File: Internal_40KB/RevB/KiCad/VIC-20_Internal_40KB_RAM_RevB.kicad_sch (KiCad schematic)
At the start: 17 parts, among them J1 BLK Decoder, J2 RAM Decoder, J3 Disable/Enable Switch, J4 UD4, J5 UE4, U1 74HCT138, U2 74HCT138, U3 74HCT10, U4 74HCT30, U5 74HCT157, U6 62256

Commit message: Initial Rev B design
A simple extension of the 32KB expansion by adding a 6264 piggybacked on top of the 62256 and routing the ~BLK5 select to it.
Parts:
- added J6: 20, Connector_PinHeader_2.54mm:PinHeader_1x01_P2.54mm_Vertical, symbol Connector_Generic:Conn_01x01
- added J7: 26, Connector_PinHeader_2.54mm:PinHeader_1x01_P2.54mm_Vertical, symbol Connector_Generic:Conn_01x01
- added U7: 6264 SRAM, Package_DIP:DIP-28_W15.24mm, symbol Memory_RAM:HY6264AxP
- C3: value 100nF -> 200nF
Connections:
- net +5V: now also J7.1 (Pin_1), U7.26 (CS2), U7.28 (VCC); no longer U5.14 (I0d)
- net BD0: now also U7.11 (I/O0)
- net BD1: now also U7.12 (I/O1)
- net BD2: now also U7.13 (I/O2)
- net BD3: now also U7.15 (I/O3)
- net BD4: now also U7.16 (I/O4)
- net BD5: now also U7.17 (I/O5)
- net BD6: now also U7.18 (I/O6)
- net BD7: now also U7.19 (I/O7)
- net GND: now also U7.14 (GND)
- net VA0: now also U7.10 (A0)
- net VA1: now also U7.9 (A1)
- net VA10: now also U7.21 (A10)
- net VA11: now also U7.23 (A11)
- net VA12: now also U7.2 (A12)
- net VA2: now also U7.8 (A2)
- net VA3: now also U7.7 (A3)
- net VA4: now also U7.6 (A4)
- net VA5: now also U7.5 (A5)
- net VA6: now also U7.4 (A6)
- net VA7: now also U7.3 (A7)
- net VA8: now also U7.25 (A8)
- net VA9: now also U7.24 (A9)
- net VR/~{W}: now also U7.27 (~{WE})
- net ~{BLK5}: now also U5.14 (I0d), J6.1 (Pin_1), U7.20 (~{CS1}); no longer J1.10 (Pin_10)
- net ~{OE}: now also U7.22 (~{OE})
- net ~{BLK5_{OUT}}: now reaches U5.12 (Zd)
- net ~{BLK5_{OUT}}: now also J1.10 (Pin_10)
- no-connect marks 25 -> 24
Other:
- note removed: "Add ~{BLK5} with additional 6264 in future?"
- title: Commodore VIC-20 32KB RAM Expansion  -> Commodore VIC-20 32+3KB RAM Expansion 
- moved on the sheet: C1, C2, C3, C4, C5, U3B, U3C, U3D, U4B, U5, U6

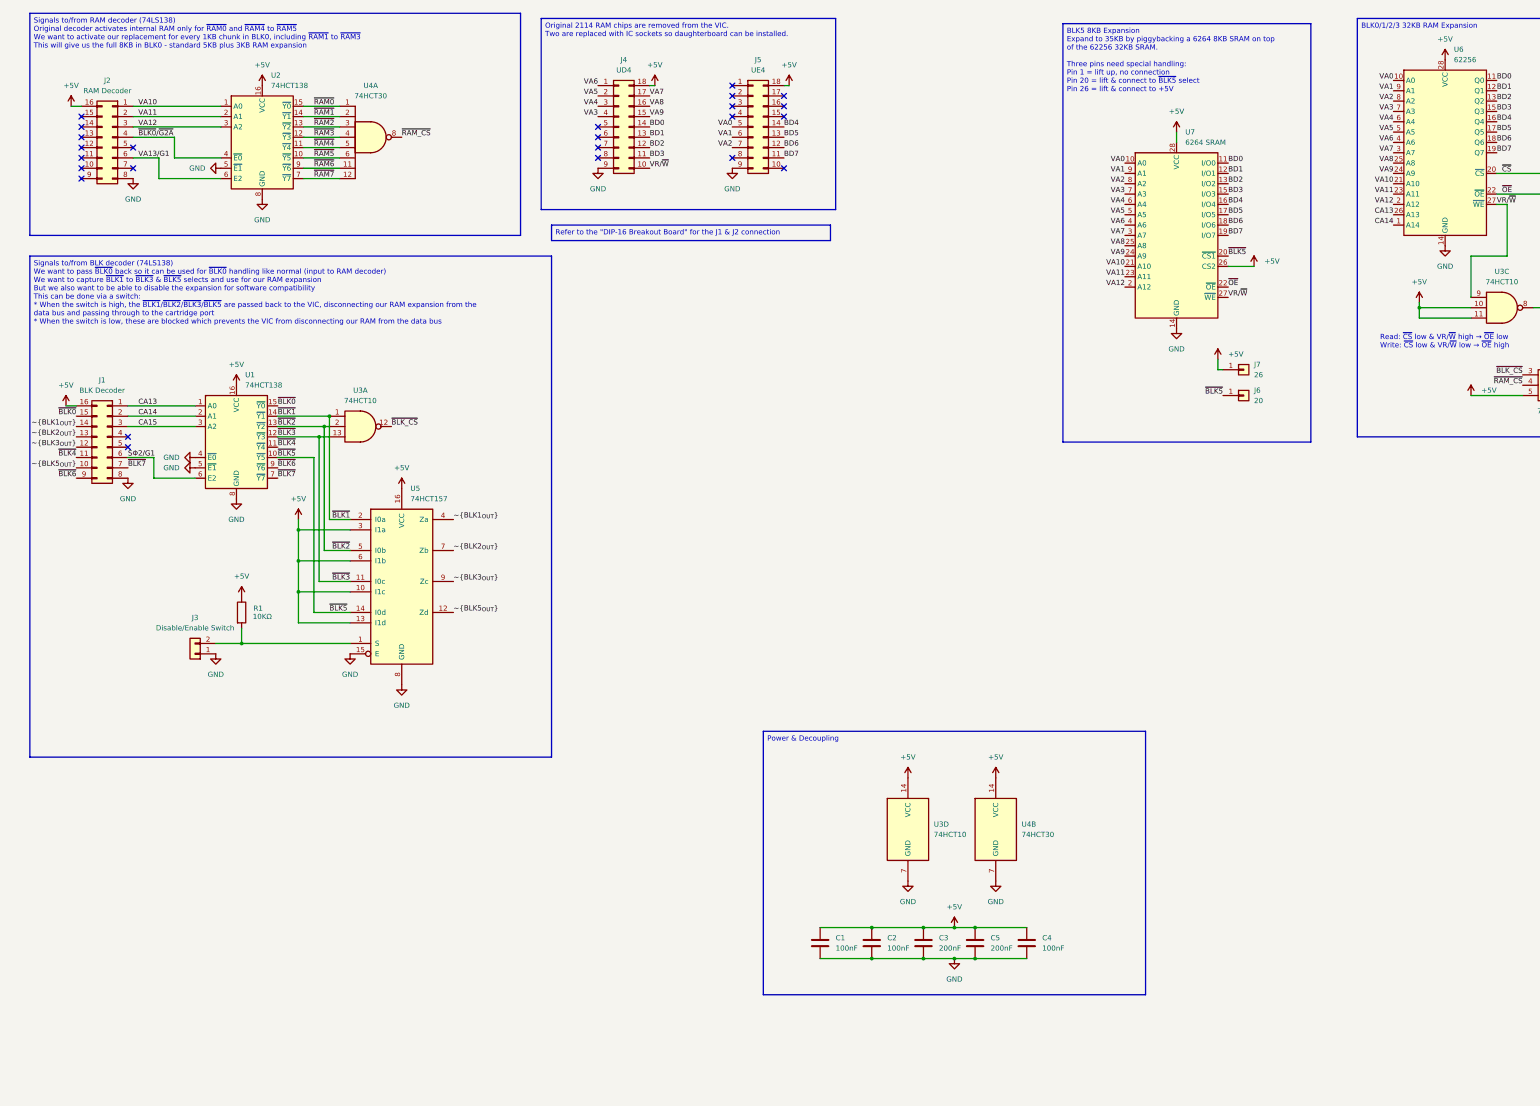
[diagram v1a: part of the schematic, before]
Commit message: Added +3KB disable switch
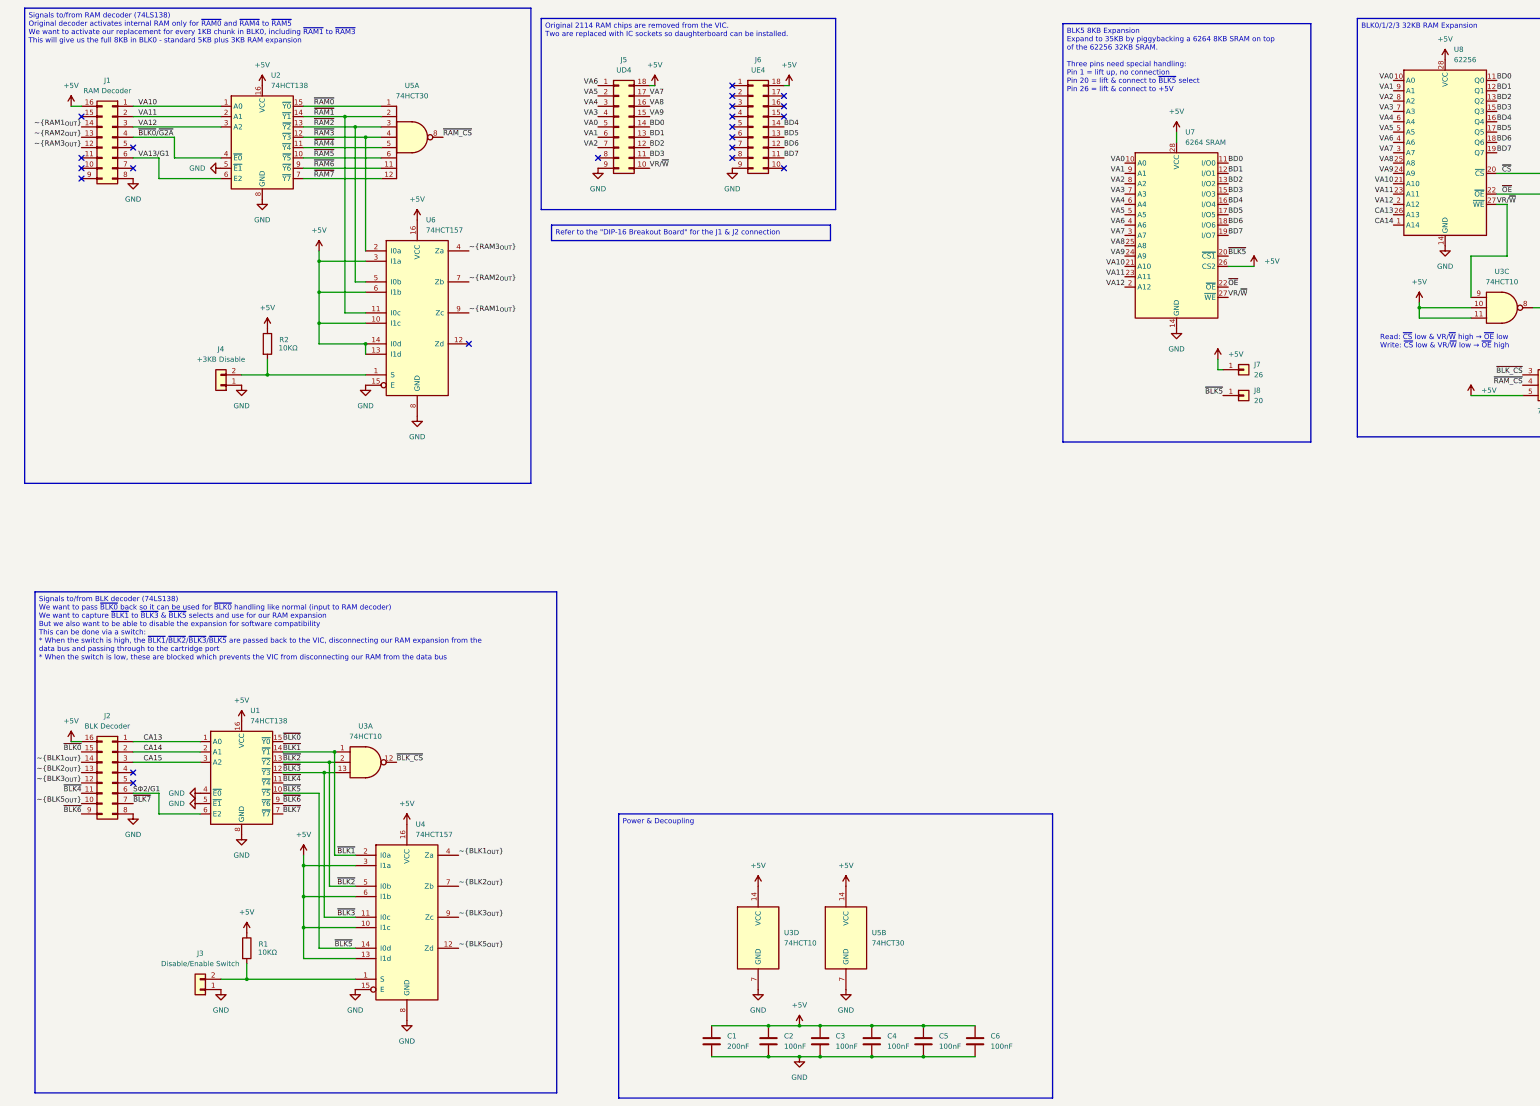
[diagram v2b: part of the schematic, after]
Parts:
- removed C2: 100nF, Capacitor_THT:C_Disc_D3.0mm_W2.0mm_P2.50mm, symbol Device:C
- added C5, C6: 100nF, Capacitor_THT:C_Disc_D3.0mm_W2.0mm_P2.50mm, symbol Device:C
- added J4: +3KB Disable, Connector_PinHeader_2.54mm:PinHeader_1x02_P2.54mm_Vertical, symbol Connector_Generic:Conn_01x02
- added R2: 10KΩ, Resistor_THT:R_Axial_DIN0207_L6.3mm_D2.5mm_P7.62mm_Horizontal, symbol Device:R
- added U6: 74HCT157, Package_DIP:DIP-16_W7.62mm, symbol 74xx:74LS157
- C1: value 100nF -> 200nF
- C2: renamed from C3; value 200nF -> 100nF
- C3: renamed from C5; value 200nF -> 100nF
- renumbered J2 to J1, J1 to J2, J4 to J5, J5 to J6, J6 to J8, U5 to U4, U4 to U5, U6 to U8
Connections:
- net +5V: now also C5.1, C6.1, R2.1, U6.10 (I1c), U6.13 (I1d), U6.14 (I0d), U6.16 (VCC), U6.3 (I1a), U6.6 (I1b)
- net GND: now also C5.2, C6.2, J4.1 (Pin_1), U6.15 (E), U6.8 (GND)
- net VA0: now also J5.5 (Pin_5); no longer J6.5 (Pin_5)
- net VA1: now also J5.6 (Pin_6); no longer J6.6 (Pin_6)
- net VA2: now also J5.7 (Pin_7); no longer J6.7 (Pin_7)
- net ~{RAM1}: now also U6.11 (I0c)
- net ~{RAM2}: now also U6.5 (I0b)
- net ~{RAM3}: now also U6.2 (I0a)
- net ~{RAM3_{OUT}}: now reaches J1.12 (Pin_12)
- net ~{RAM3_{OUT}}: now also U6.4 (Za)
- net ~{RAM2_{OUT}}: now reaches J1.13 (Pin_13)
- net ~{RAM2_{OUT}}: now also U6.7 (Zb)
- net ~{RAM1_{OUT}}: now reaches J1.14 (Pin_14)
- net ~{RAM1_{OUT}}: now also U6.9 (Zc)
- new net: J4.2 (Pin_2), R2.2, U6.1 (S)
- no-connect marks 24 -> 22
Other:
- moved on the sheet: C1, C2, C3, C4, J2, J3, R1, U1, U3A, U3D, U4, U5A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
